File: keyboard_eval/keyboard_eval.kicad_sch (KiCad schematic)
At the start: 65 parts, among them IC1 IS31FL3733B-TQLS4, J1 Conn_01x03, J2 Conn_01x04, J3 Conn_01x04, J4 Conn_01x07, J5 Conn_01x03, J6 Conn_01x03, J7 Conn_01x06, SW1 RotaryEncoder_Switch

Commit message: WIP layout
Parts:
- removed JP2, JP3: Jumper_3_Open, Jumper:SolderJumper-3_P1.3mm_Open_RoundedPad1.0x1.5mm, symbol Jumper:Jumper_3_Open
- added JP2, JP3, JP4: Jumper_2_Open, Jumper:SolderJumper-2_P1.3mm_Open_RoundedPad1.0x1.5mm, symbol Jumper:Jumper_2_Open
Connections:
- net +5V: now also JP4.1 (A)
- net LED_SCL: now also JP2.1 (A)
- net LED_SDA: now also JP3.1 (A)
- net OLED_SCL: now also J3.3 (Pin_3), JP3.2 (B)
- net OLED_SDA: now also J3.4 (Pin_4), JP2.2 (B)
- net VCC: now also JP4.2 (B)
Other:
- note added: "5V-VCC connection (use if VCC=5V)"
- note added: "OLED I2C Input Connector"
- note removed: "OLED I2C Connector"
- moved on the sheet: J5, J6

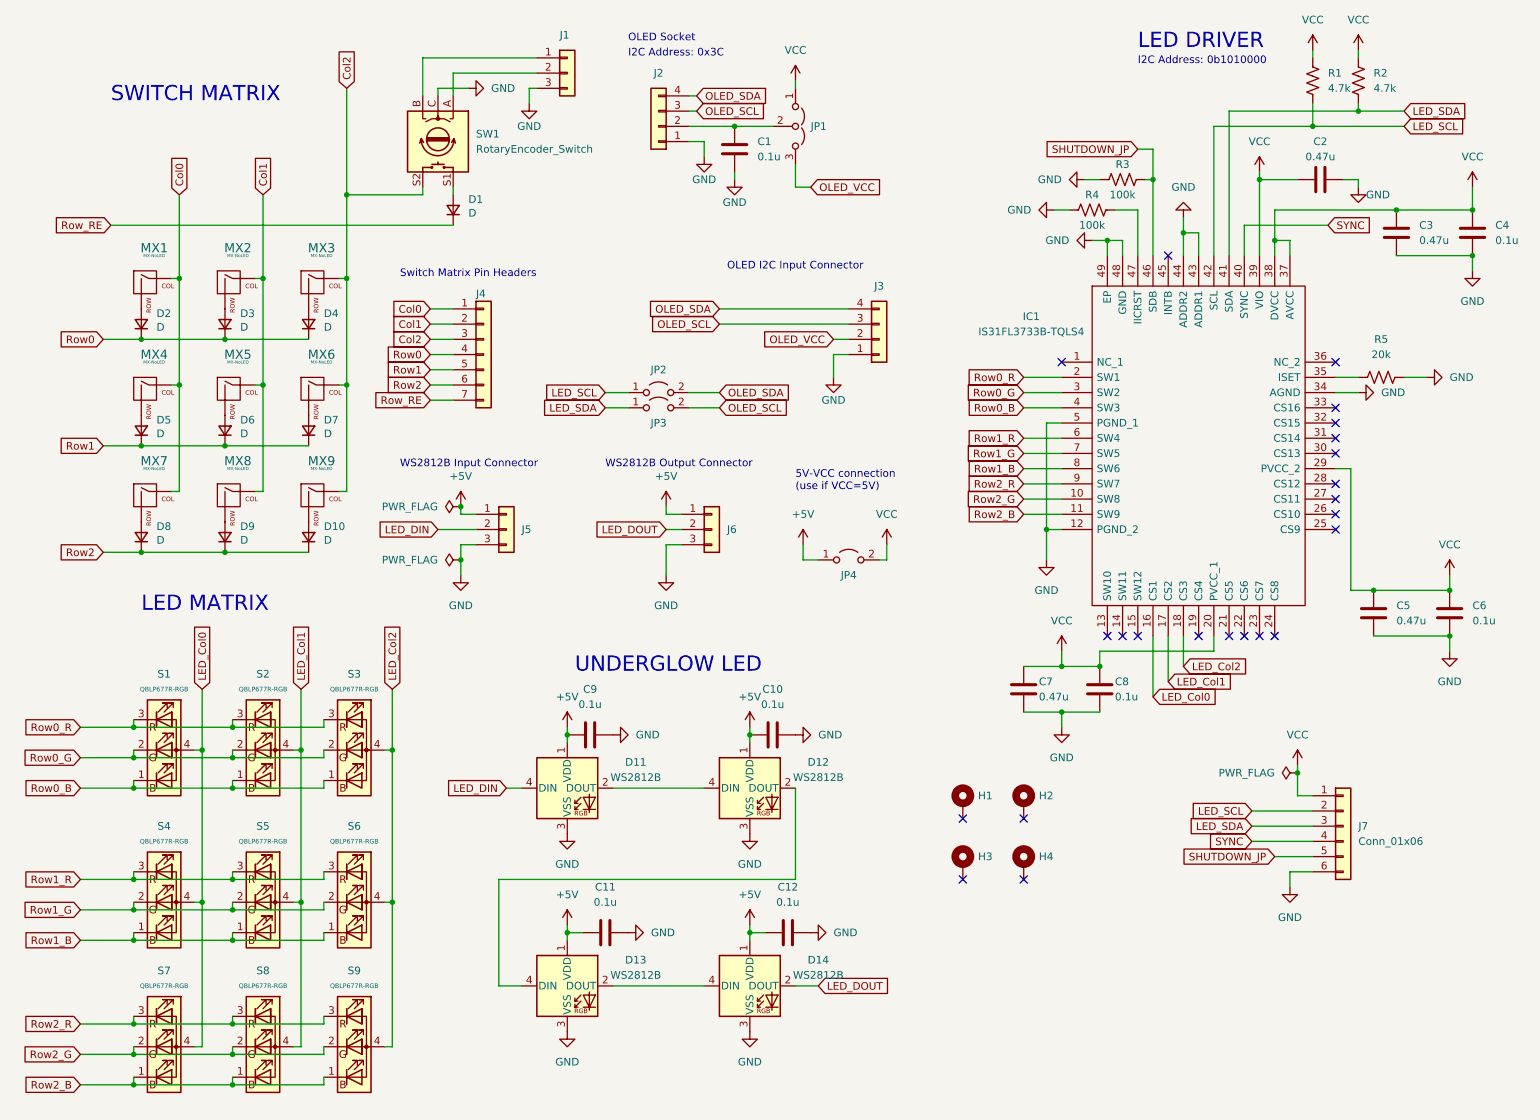
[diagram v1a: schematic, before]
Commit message: Finished initial layout
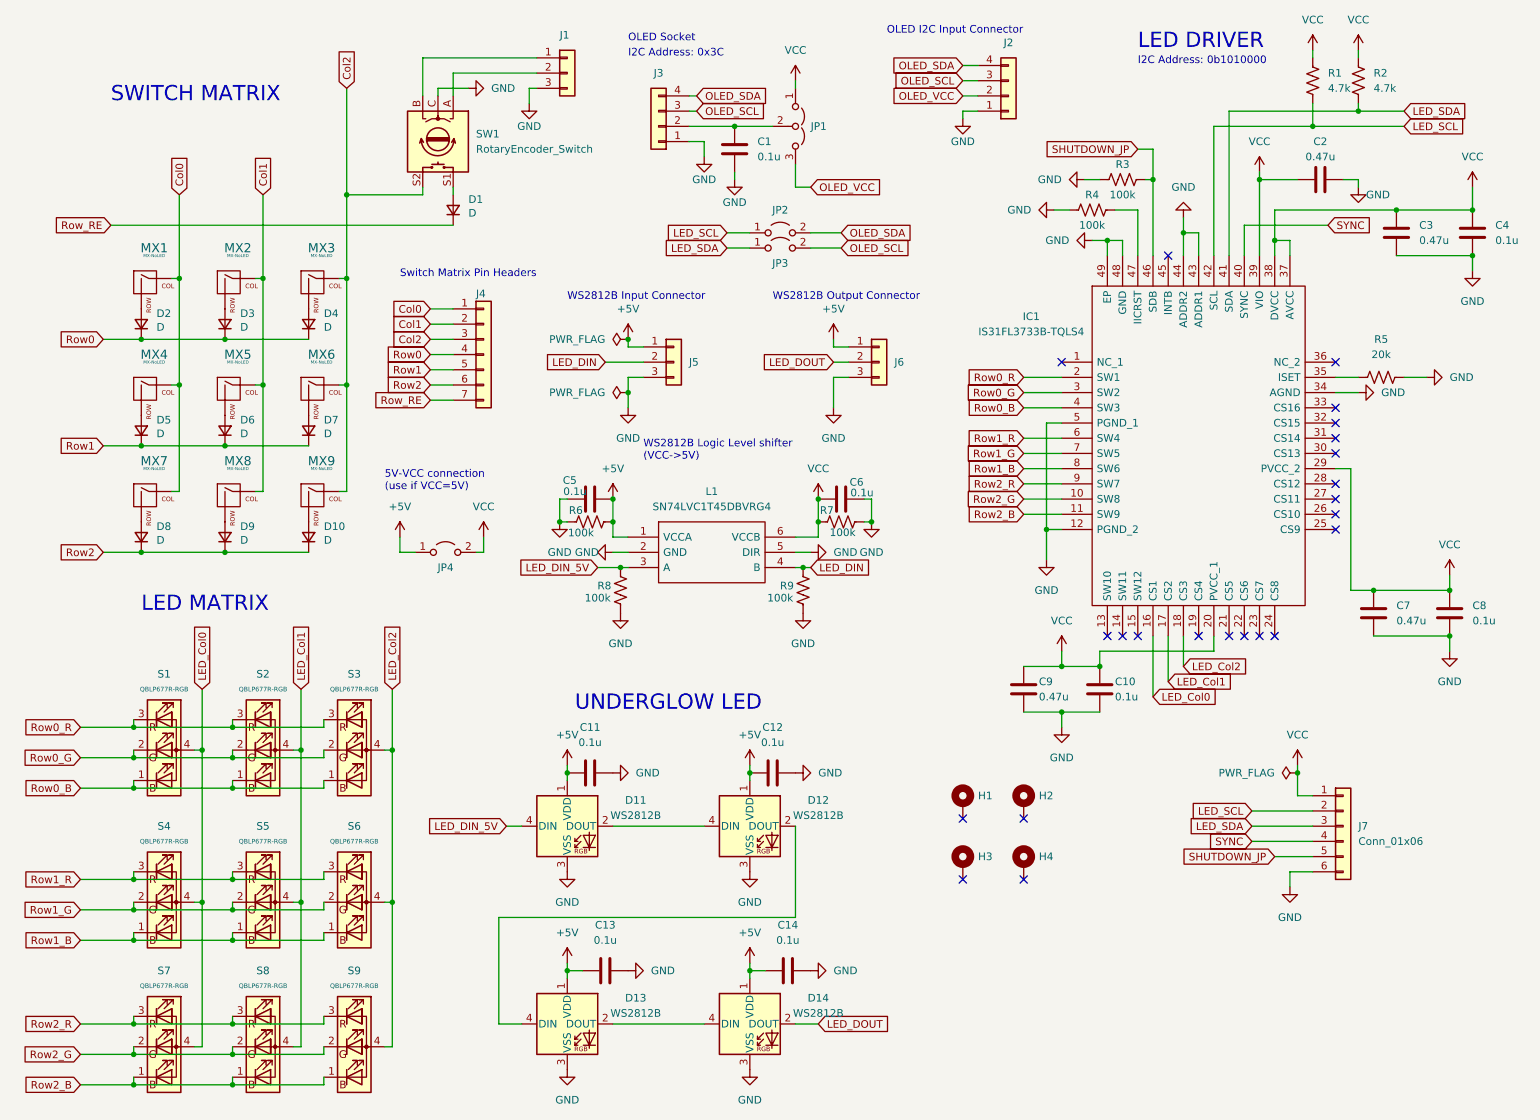
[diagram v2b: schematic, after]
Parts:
- added C5, C6: 0.1u, Capacitor_SMD:C_0603_1608Metric_Pad1.08x0.95mm_HandSolder, symbol Device:C
- added L1: SN74LVC1T45DBVRG4, SOT95P280X145-6N, symbol SamacSys_Parts:SN74LVC1T45DBVRG4
- added R6, R7, R8, R9: 100k, Resistor_SMD:R_0603_1608Metric_Pad0.98x0.95mm_HandSolder, symbol Device:R_US
- renumbered C8 to C10, C9 to C11, C10 to C12, C11 to C13, C12 to C14, C5 to C7, C6 to C8, C7 to C9, J3 to J2, J2 to J3
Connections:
- net +5V: now also C5.2, L1.1 (VCCA), R6.1
- net GND: now also C5.1, C6.2, L1.2 (GND), L1.5 (DIR), R6.2, R7.1, R8.1, R9.1
- net LED_DIN: now also L1.4 (B), R9.2; no longer D11.4 (DIN)
- net VCC: now also C6.1, L1.6 (VCCB), R7.2
- new net LED_DIN_5V: D11.4 (DIN), L1.3 (A), R8.2
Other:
- note added: "WS2812B Logic Level shifter (VCC->5V)"
- moved on the sheet: C11, C12, C13, C14, D11, D12, D13, D14, J2, J5, J6, JP2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

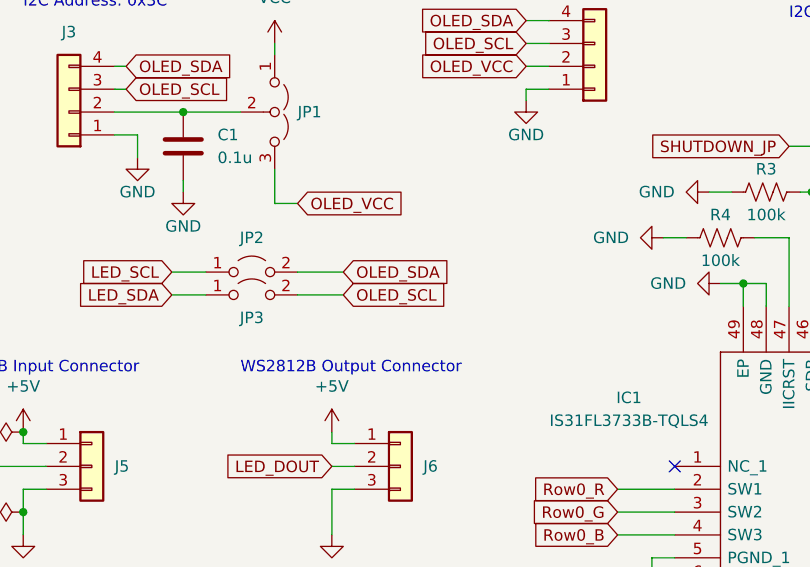
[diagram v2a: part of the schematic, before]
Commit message: Fixing schematics and firmware
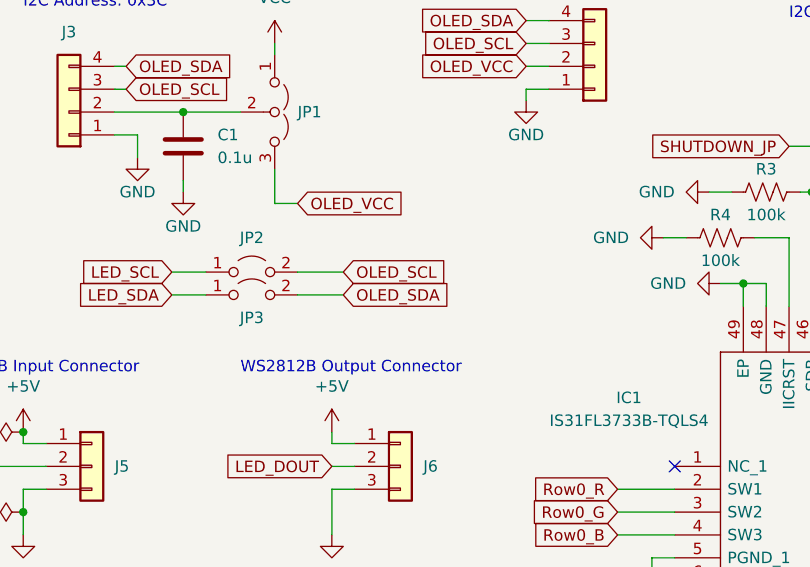
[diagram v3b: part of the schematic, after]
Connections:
- net OLED_SCL: now also JP2.2 (B); no longer JP3.2 (B)
- net OLED_SDA: now also JP3.2 (B); no longer JP2.2 (B)
